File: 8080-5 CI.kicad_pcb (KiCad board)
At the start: 2 copper layers, 50 x 50 mm, 14 parts, among them J1 Conn_02x18_Counter_Clockwise, U1 74HCT595, U2 74HCT595, U3 74HCT595, U4 74HCT165

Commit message: Add files via upload
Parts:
- removed the C1 at (109.4, 111.7)
- removed the C2 at (109.4, 125.9)
- removed the C3 at (104.6, 99.1)
- removed C8: 1u, Capacitor_Tantalum_SMD:CP_EIA-3216-18_Kemet-A_Pad1.58x1.35mm_HandSolder
- added C5: 100n, Capacitor_SMD:C_0805_2012Metric_Pad1.18x1.45mm_HandSolder, B.Cu at (98.6, 109.2)
- added R1: 1k, Resistor_SMD:R_0805_2012Metric_Pad1.20x1.40mm_HandSolder, B.Cu at (95.3, 111.8)
- added R2: 1k, Resistor_SMD:R_0805_2012Metric_Pad1.20x1.40mm_HandSolder, B.Cu at (95.3, 116.8)
- added R3: 1k, Resistor_SMD:R_0805_2012Metric_Pad1.20x1.40mm_HandSolder, B.Cu at (95.3, 121.9)
- added R4: 1k, Resistor_SMD:R_0805_2012Metric_Pad1.20x1.40mm_HandSolder, B.Cu at (96.4, 124.5)
- added U5: 74HCT165, Package_DIP:DIP-16_W7.62mm_LongPads, F.Cu at (108.0, 141.4)
- U3: value 74HCT595 -> 74HCT06; footprint Package_DIP:DIP-16_W7.62mm_LongPads -> Package_DIP:DIP-14_W7.62mm_LongPads
- U4: value 74HCT165 -> 74HCT595
- moved U3 23.5 mm to (92.0, 111.8), turned to 0 degrees
- moved U4 12.3 mm to (108.0, 129.1)
- moved C2 1.58 mm to (108.0, 112.5), turned to 90 degrees
- moved C4 1.40 mm to (108.0, 124.9), turned to 90 degrees
- moved C3 0.05 mm to (109.0, 136.4)
- renumbered C4 to C1, C5 to C2, C7 to C3, C6 to C4
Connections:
- A1 pad 19: /~{MEMR_Out} -> Net-(A1-A0)
- A1 pad 20: /~{MEMW_Out} -> Net-(A1-A1)
- A1 pad 21: /~{IOR_Out} -> Net-(A1-A2)
- A1 pad 22: /~{IOW_Out} -> Net-(A1-A3)
- U3 pad 1: /D1 -> Net-(A1-A3)
- U3 pad 10: /+5V -> GND
- U3 pad 11: /DataShift_Out_Clk -> GND
- U3 pad 12: /DataShift_Out_Latch -> GND
- U3 pad 13: /Data_Out_En -> GND
- U3 pad 14: Net-(U2-QH') -> /+5V
- U3 pad 2: /D2 -> /~{MEMR_Out}
- U3 pad 3: /D3 -> Net-(A1-A2)
- U3 pad 4: /D4 -> /~{MEMW_Out}
- U3 pad 5: /D5 -> Net-(A1-A1)
- U3 pad 6: /D6 -> /~{IOR_Out}
- U3 pad 7: /D7 -> GND
- U3 pad 8: GND -> /~{IOW_Out}
- U3 pad 9: unconnected-(U3-QH'-Pad9) -> Net-(A1-A0)
- U4 pad 1: /DataShift_In_Latch -> /D1
- U4 pad 10: GND -> /+5V
- U4 pad 11: /D0 -> /DataShift_Out_Clk
- U4 pad 12: /D1 -> /DataShift_Out_Latch
- U4 pad 13: /D2 -> /Data_Out_En
- U4 pad 14: /D3 -> Net-(U2-QH')
- U4 pad 15: GND -> /D0
- U4 pad 2: /DataShift_In_Clk -> /D2
- U4 pad 3: /D4 -> /D3
- U4 pad 4: /D5 -> /D4
- U4 pad 5: /D6 -> /D5
- U4 pad 6: /D7 -> /D6
- U4 pad 7: unconnected-(U4-~{Q7}-Pad7) -> /D7
- U4 pad 9: /DataShift_In -> unconnected-(U4-QH'-Pad9)
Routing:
- net Net-(A1-A0): track 0.00 -> 24.9 mm
- net /+5V: track 144.7 -> 162.4 mm
- net Net-(A1-A1): track 0.00 -> 16.3 mm
- net Net-(A1-A3): track 0.00 -> 11.1 mm
- net Net-(A1-A2): track 0.00 -> 6.61 mm
- net /D1: track 35.6 -> 42.0 mm
- net /~{IOW_Out}: track 82.8 -> 88.4 mm
- net /~{IOR_Out}: track 94.2 -> 90.2 mm
- net /~{BUSEn_Out}: track 89.3 -> 85.6 mm
- net /DataShift_Out: track 20.1 -> 21.3 mm
- net /~{MEMW_Out}: track 96.2 -> 95.2 mm
- net /DataShift_In_Clk: track 21.1 -> 21.7 mm
- net /D2: track 28.3 -> 27.7 mm
- net GND: vias 158 -> 187

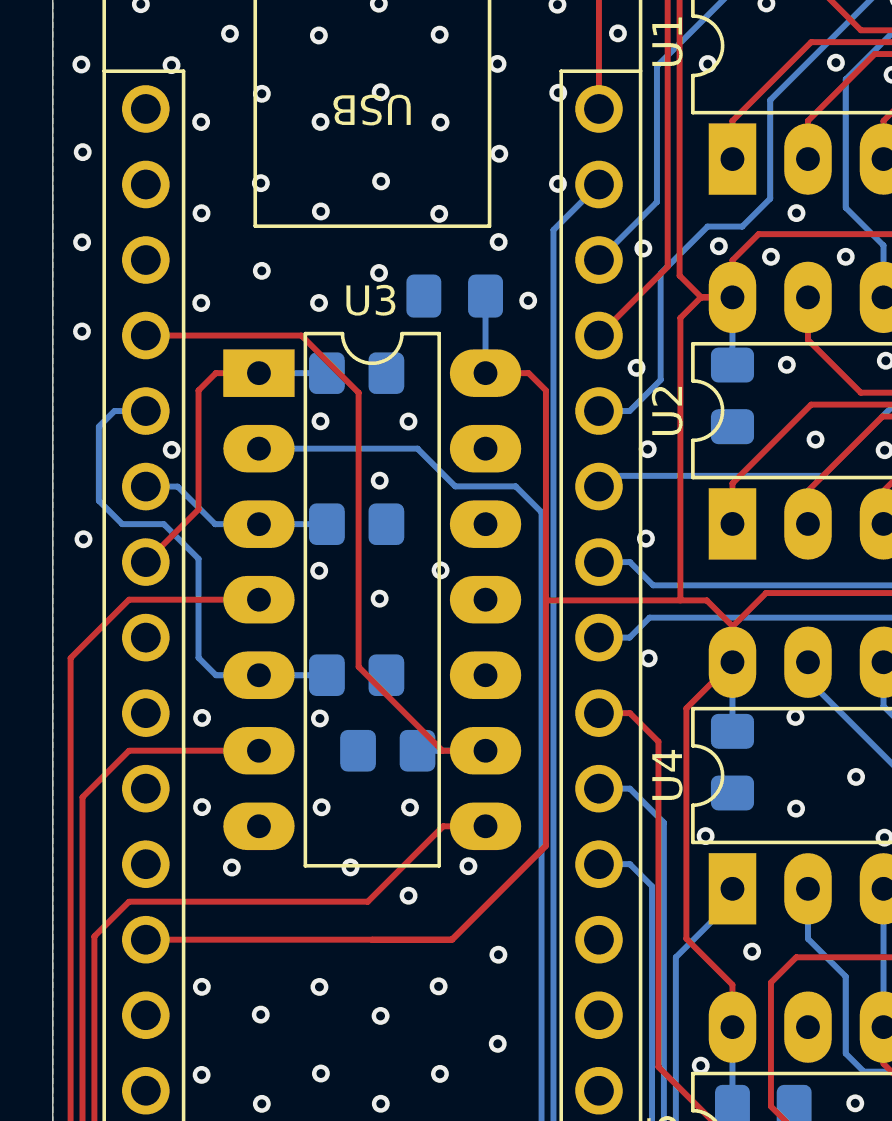
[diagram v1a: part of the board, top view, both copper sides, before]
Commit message: Add Arduino firmware (test version), fix schematic
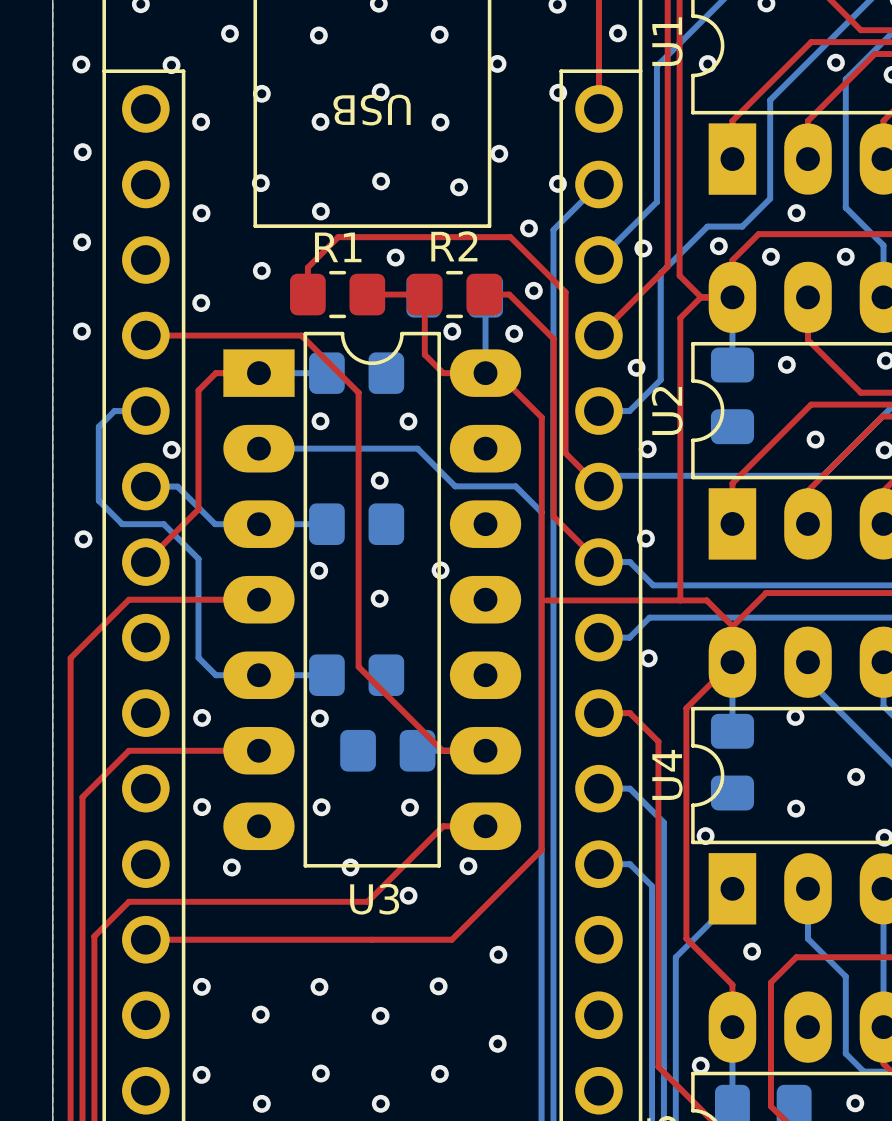
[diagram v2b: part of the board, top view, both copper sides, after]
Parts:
- added R1: 1k, Resistor_SMD:R_0805_2012Metric_Pad1.20x1.40mm_HandSolder, F.Cu at (94.7, 109.1)
- added R2: 1k, Resistor_SMD:R_0805_2012Metric_Pad1.20x1.40mm_HandSolder, F.Cu at (98.6, 109.1)
- renumbered R1 to R3, R2 to R4, R3 to R5, R4 to R6
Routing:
- net /Address_Out_En: track 28.9 -> 46.7 mm
- net /Data_Out_En: track 14.1 -> 25.2 mm
- net /+5V: track 162.4 -> 160.8 mm
- net GND: vias 187 -> 188
